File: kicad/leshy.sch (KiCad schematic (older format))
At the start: 34 parts, among them J1 USER_SW, J2 SD_SW, J3 IDD, K1 SWD, K2 MICROSD_TFP09-2-12B, K3 VIN, K4 B1_18, SW1 RESET, SW2 PA0, U1 STM32F030F4P6, U2 1117-3.3, U3 MCP1700-3302

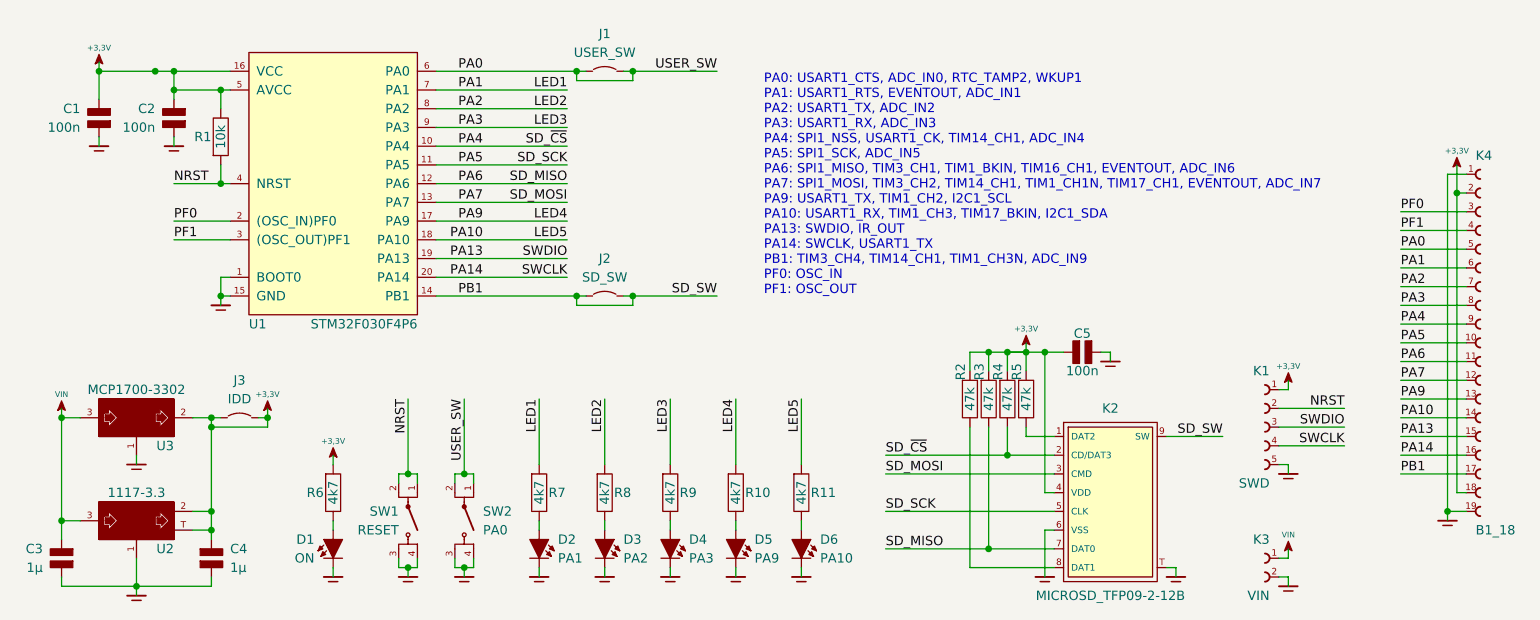
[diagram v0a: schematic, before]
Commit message: Add new board revision
Main differences are:
- The SD card now has a MOSFET, so it can be completely shut off
- More (hopefully useful) silkscreen text
- Logo on board
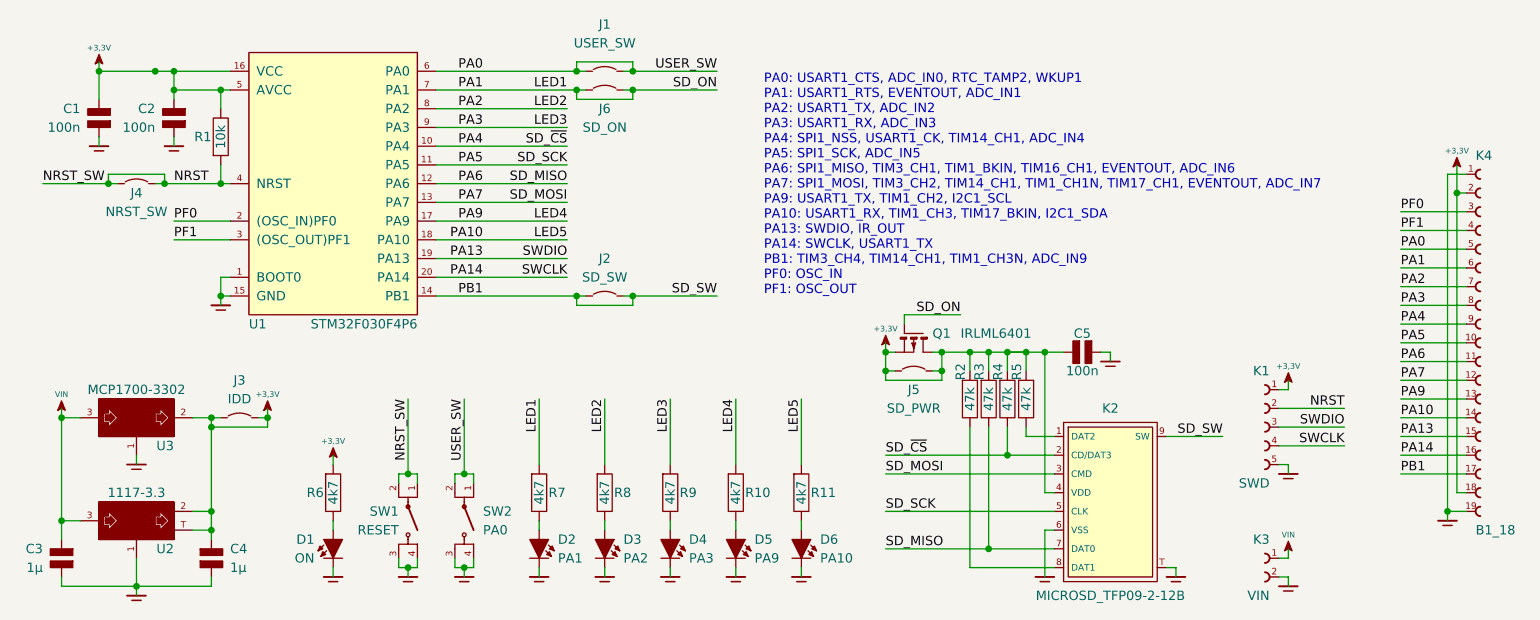
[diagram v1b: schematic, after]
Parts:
- added J4: NRST_SW, rcl:SOLDER_JUMPER_0603_B, symbol JUMPER
- added J5: SD_PWR, rcl:SOLDER_JUMPER_0603_B, symbol JUMPER
- added J6: SD_ON, rcl:SOLDER_JUMPER_0603_B, symbol JUMPER
- added Q1: IRLML6401, sot:SOT23, symbol IRLML6401
- J1, J2: footprint rcl:0603_B -> rcl:SOLDER_JUMPER_0603_B
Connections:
- net +3,3V: now also J5.1, J5.2, Q1.2 (S), Q1.3 (D)
- net LED1: now also J6.1, J6.2, Q1.1 (G)
- net NRST: now also J4.1, J4.2
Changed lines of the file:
@@
 LIBS:triac
 LIBS:xilinx
-LIBS:stm32f0board-cache
+LIBS:leshy-cache
 EELAYER 25 0
 EELAYER END
@@
 	7000 3700 7000 2950
 Wire Wire Line
-	6600 2950 7100 2950
+	6400 2950 7100 2950
 Wire Wire Line
 	6800 2950 6900 2950
@@
 	6800 2950 6800 3050
 Connection ~ 6700 2950
-Wire Wire Line
-	6900 2900 6900 3050
 Connection ~ 6800 2950
 $Comp
@@
 L +3,3V #PWR04
 U 1 1 57D32088
-P 6900 2900
-F 0 "#PWR04" H 6900 2825 30  0001 C CNN
-F 1 "+3,3V" H 6900 2975 30  0000 C CNN
-F 2 "" H 6900 2900 50  0001 C CNN
-F 3 "" H 6900 2900 60  0000 C CNN
-	1    6900 2900
+P 6150 2900
+F 0 "#PWR04" H 6150 2825 30  0001 C CNN
+F 1 "+3,3V" H 6150 2975 30  0000 C CNN
+F 2 "" H 6150 2900 50  0001 C CNN
+F 3 "" H 6150 2900 60  0000 C CNN
+	1    6150 2900
 	1    0    0    -1
 $EndComp
@@
 Connection ~ 2600 1550
 Wire Wire Line
-	2600 1950 2600 2050
-Wire Wire Line
-	2350 2050 2650 2050
+	2600 2050 2600 1950
+Wire Wire Line
+	2250 2050 2650 2050
 $Comp
 L C C2
@@
 	3650 3600 3650 3650
 Text Label 3600 3200 3    50   ~ 0
-NRST
+NRST_SW
 Wire Wire Line
 	3600 3200 3600 3600
@@
 	3750 1450 4550 1450
 Wire Wire Line
-	3750 1550 4450 1550
-Wire Wire Line
 	3750 1650 4450 1650
 Wire Wire Line
@@
 F 0 "J2" H 4650 2850 50  0000 C CNN
 F 1 "SD_SW" H 4650 2750 50  0000 C CNN
-F 2 "rcl:0603_B" H 4550 2650 50  0001 C CNN
+F 2 "rcl:SOLDER_JUMPER_0603_B" H 4550 2650 50  0001 C CNN
 F 3 "" H 4650 2650 60  0000 C CNN
 	1    4650 2650
@@
 Wire Wire Line
 	4500 2650 4500 2700
-Wire Wire Line
-	4500 2700 4800 2700
 Wire Wire Line
 	4800 2700 4800 2650
@@
 U 1 1 57E01293
 P 4650 1450
-F 0 "J1" H 4650 1650 50  0000 C CNN
-F 1 "USER_SW" H 4650 1550 50  0000 C CNN
-F 2 "rcl:0603_B" H 4550 1450 50  0001 C CNN
+F 0 "J1" H 4650 1700 50  0000 C CNN
+F 1 "USER_SW" H 4650 1600 50  0000 C CNN
+F 2 "rcl:SOLDER_JUMPER_0603_B" H 4550 1450 50  0001 C CNN
 F 3 "" H 4650 1450 60  0000 C CNN
 	1    4650 1450
@@
 $EndComp
 Wire Wire Line
-	4500 1450 4500 1500
-Wire Wire Line
-	4500 1500 4800 1500
-Wire Wire Line
-	4800 1500 4800 1450
+	4500 1450 4500 1400
+Wire Wire Line
+	4500 1400 4800 1400
+Wire Wire Line
+	4800 1400 4800 1450
 Wire Wire Line
 	4750 1450 5250 1450
@@
 Connection ~ 2550 3900
 Wire Wire Line
-	2600 3300 2450 3300
+	2450 3300 2600 3300
 Connection ~ 2550 3300
 Wire Wire Line
@@
 Connection ~ 2550 3350
 Connection ~ 2850 3300
+Wire Wire Line
+	6900 2950 6900 3050
+$Comp
+L JUMPER J4
+U 1 1 58F7ADD8
+P 2150 2050
+F 0 "J4" H 2150 2000 50  0000 C CNN
+F 1 "NRST_SW" H 2150 1900 50  0000 C CNN
+F 2 "rcl:SOLDER_JUMPER_0603_B" H 2050 2050 50  0001 C CNN
+F 3 "" H 2150 2050 60  0000 C CNN
+	1    2150 2050
+	1    0    0    -1
+$EndComp
+Text Label 1650 2050 0    50   ~ 0
+NRST_SW
+Wire Wire Line
+	1650 2050 2050 2050
+Wire Wire Line
+	2000 2050 2000 2000
+Wire Wire Line
+	2000 2000 2300 2000
+Wire Wire Line
+	2300 2000 2300 2050
+Connection ~ 2300 2050
+Connection ~ 2000 2050
+$Comp
+L IRLML6401 Q1
+U 1 1 58F7B77E
+P 6300 2900
+F 0 "Q1" V 6250 3000 50  0000 L CNN
+F 1 "IRLML6401" V 6250 3150 50  0000 L CNN
+F 2 "sot:SOT23" H 6400 2750 50  0001 L CNN
+F 3 "" H 6300 2900 60  0000 C CNN
+	1    6300 2900
+	0    1    1    0
+$EndComp
+Connection ~ 6600 2950
+Wire Wire Line
+	6150 2900 6150 3100
+Wire Wire Line
+	6150 2950 6200 2950
+$Comp
+L JUMPER J5
+U 1 1 58F7C21D
+P 6300 3050
+F 0 "J5" H 6300 2950 50  0000 C CNN
+F 1 "SD_PWR" H 6300 2850 50  0000 C CNN
+F 2 "rcl:SOLDER_JUMPER_0603_B" H 6200 3050 50  0001 C CNN
+F 3 "" H 6300 3050 60  0000 C CNN
+	1    6300 3050
+	1    0    0    -1
+$EndComp
+Wire Wire Line
+	6400 3050 6450 3050
+Wire Wire Line
+	6450 2950 6450 3100
+Connection ~ 6450 2950
+Wire Wire Line
+	6150 3050 6200 3050
+Connection ~ 6150 2950
+Wire Wire Line
+	6250 2800 6250 2750
+Wire Wire Line
+	6250 2750 6550 2750
+Text Label 6550 2750 2    50   ~ 0
+SD_ON
+Text Label 5250 1550 2    50   ~ 0
+SD_ON
+Wire Wire Line
+	3750 1550 4550 1550
+$Comp
+L JUMPER J6
+U 1 1 58F8B41E
+P 4650 1550
+F 0 "J6" H 4650 1450 50  0000 C CNN
+F 1 "SD_ON" H 4650 1350 50  0000 C CNN
+F 2 "rcl:SOLDER_JUMPER_0603_B" H 4550 1550 50  0001 C CNN
+F 3 "" H 4650 1550 60  0000 C CNN
+	1    4650 1550
+	1    0    0    -1
+$EndComp
+Wire Wire Line
+	4750 1550 5250 1550
+Wire Wire Line
+	6450 3100 6150 3100
+Connection ~ 6450 3050
+Connection ~ 6150 3050
+Wire Wire Line
+	4500 1550 4500 1600
+Wire Wire Line
+	4500 1600 4800 1600
+Wire Wire Line
+	4800 1600 4800 1550
+Connection ~ 4800 1550
+Connection ~ 4500 1550
+Wire Wire Line
+	4500 2700 4800 2700
 $EndSCHEMATC
